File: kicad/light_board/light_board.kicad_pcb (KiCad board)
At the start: 2 copper layers, 89 x 48 mm, 23 parts, among them J1 24V, J10 Screw_Terminal_01x02, J11 Screw_Terminal_01x02, J12 VAC, J13 NEUTRAL, J2 GND, J3 MCU_L1, J4 MCU_L2, J5 MCU_L3, J6 MCU_Bike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

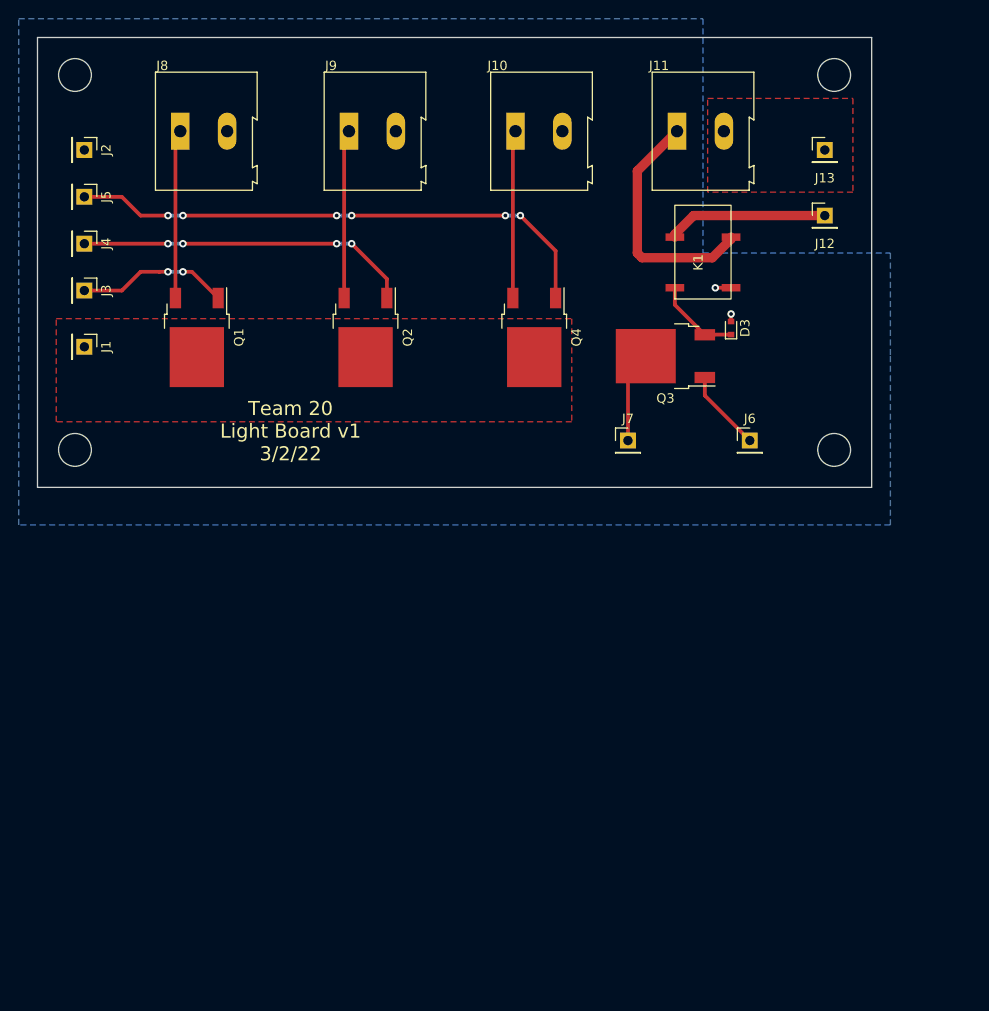
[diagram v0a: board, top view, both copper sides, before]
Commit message: added isolation to power and light boards
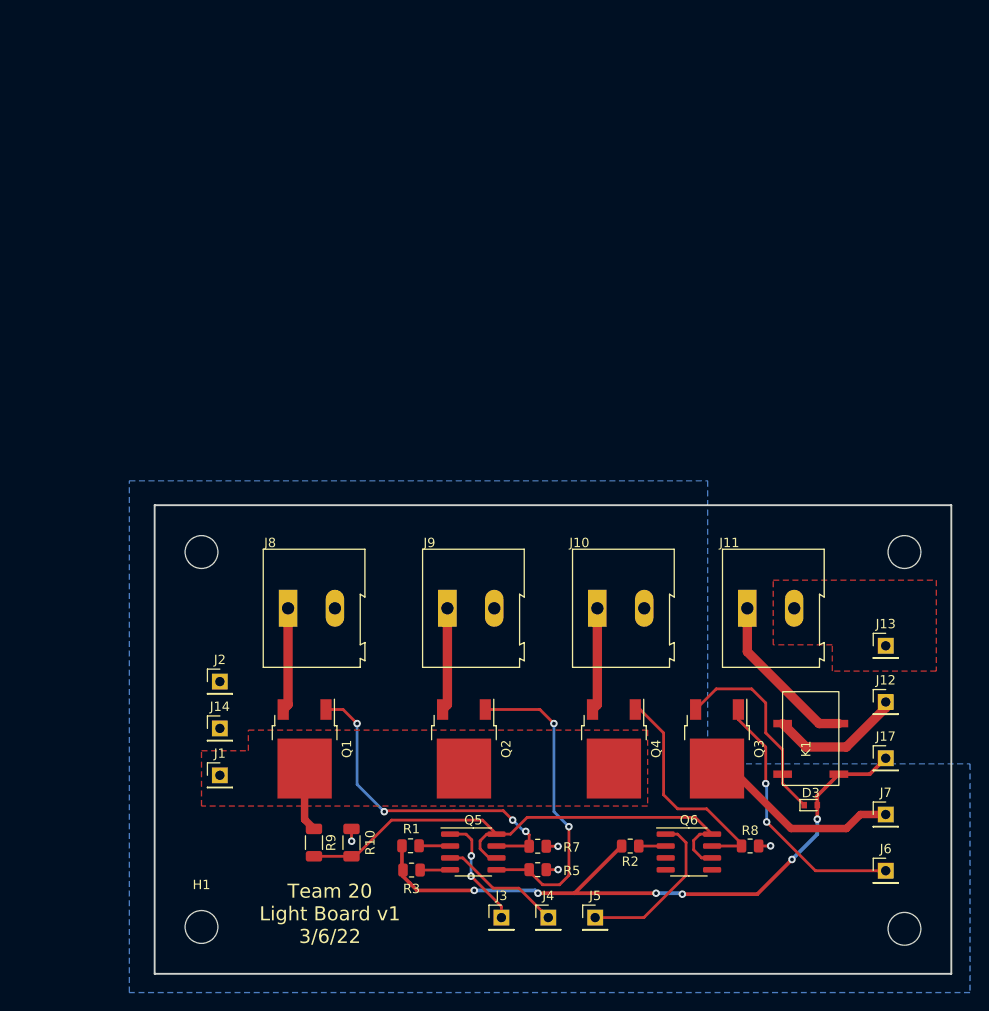
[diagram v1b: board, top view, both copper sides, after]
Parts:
- added J14: GND, Connector_PinHeader_2.54mm:PinHeader_1x01_P2.54mm_Vertical, F.Cu at (92.5, 101.7)
- added J17: MCU_GND, Connector_PinHeader_2.54mm:PinHeader_1x01_P2.54mm_Vertical, F.Cu at (163.5, 104.9)
- added Q5: MOCD207M, Package_SO:SOIC-8_3.9x4.9mm_P1.27mm, F.Cu at (119.5, 114.9)
- added Q6: MOCD207M, Package_SO:SOIC-8_3.9x4.9mm_P1.27mm, F.Cu at (142.5, 114.9)
- added R1: 10k, Resistor_SMD:R_0805_2012Metric, F.Cu at (112.8, 114.2)
- added R10: 100k, Resistor_SMD:R_1206_3216Metric, F.Cu at (106.5, 113.9)
- added R2: 10k, Resistor_SMD:R_0805_2012Metric, F.Cu at (136.2, 114.3)
- added R3: 10k, Resistor_SMD:R_0805_2012Metric, F.Cu at (112.9, 116.8)
- added R5: 10k, Resistor_SMD:R_0805_2012Metric, F.Cu at (126.4, 116.8)
- added R7: 10k, Resistor_SMD:R_0805_2012Metric, F.Cu at (126.4, 114.3)
- added R8: 10k, Resistor_SMD:R_0805_2012Metric, F.Cu at (149.0, 114.3)
- added R9: 100k, Resistor_SMD:R_1206_3216Metric, F.Cu at (102.5, 113.9)
- J7: value 5V -> MCU_5V
- Q3: value BSP89 -> FDD8453LZ
- moved H2 102.1 mm to (165.5, 82.9)
- moved J5 94.3 mm to (132.5, 121.9), turned to 0 degrees
- moved J4 87.3 mm to (127.5, 121.9), turned to 0 degrees
- moved H3 84.5 mm to (90.5, 82.9)
- moved J3 80.3 mm to (122.5, 121.9), turned to 0 degrees
- moved J2 58.5 mm to (92.5, 96.7), turned to 0 degrees
- moved J13 53.3 mm to (163.5, 92.9)
- moved K1 53.2 mm to (155.5, 103.9)
- moved H1 52.7 mm to (90.5, 122.9)
- moved J12 52.3 mm to (163.5, 98.9)
- moved J8 52.2 mm to (99.7, 88.9)
- moved J9 52.0 mm to (116.7, 88.9)
- moved H4 51.6 mm to (165.5, 123.1)
- moved J10 51.6 mm to (132.7, 88.9)
- moved D3 51.6 mm to (155.5, 109.9), turned to 0 degrees
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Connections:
- net Bike renamed MCU_Bike
- D3 pad 2: GND -> GND1
- J11 pad 2: GND1 -> Earth
- J13 pad 1: GND1 -> Earth
- J3 pad 1: L1 -> MCU_L1
- J4 pad 1: L2 -> MCU_L2
- J5 pad 1: L3 -> MCU_L3
- K1 pad 6: GND -> GND1
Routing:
- net GND1: track 0.00 -> 71.1 mm, vias 0 -> 6
- net 12V: track 0.00 -> 56.8 mm
- net L3: track 57.7 -> 24.5 mm, vias 6 -> 0
- net L1: track 16.3 -> 35.8 mm, vias 2 -> 4
- net MCU_Bike: track 8.71 -> 28.1 mm, vias 0 -> 2
- net MCU_L3: track 0.00 -> 17.6 mm
- net MCU_L2: track 0.00 -> 13.1 mm
- net Net-(D3-Pad1): track 9.15 -> 21.6 mm
- net MCU_L1: track 0.00 -> 12.2 mm, vias 0 -> 2
- net +5V: track 9.79 -> 21.3 mm
- net Net-(J11-Pad1): track 26.0 -> 17.6 mm
- net Net-(J9-Pad1): track 18.0 -> 11.0 mm
- net Net-(J8-Pad1): track 18.0 -> 11.0 mm
- net Net-(J10-Pad1): track 17.9 -> 11.0 mm
- net +24V: track 0.00 -> 6.85 mm
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- added copper zone on F.Cu, net Earth
- removed copper zone on F.Cu, net GND1
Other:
- board size 89 x 48 mm -> 85 x 50 mm
- board text added: "Team 20 Light Board v1 3/6/22"
- board text removed: "Team 20 Light Board v1 3/2/22"
